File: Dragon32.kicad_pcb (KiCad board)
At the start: 2 copper layers, 253 x 169.1 mm, 142 parts, among them IC1 4164, IC15 MC6883, IC16 74LS244N, IC17 27C256, IC18 74LS08, IC19 MC6809E, IC2 4164, IC20 MC14529B, IC24 74LS244N, IC25 LM393P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

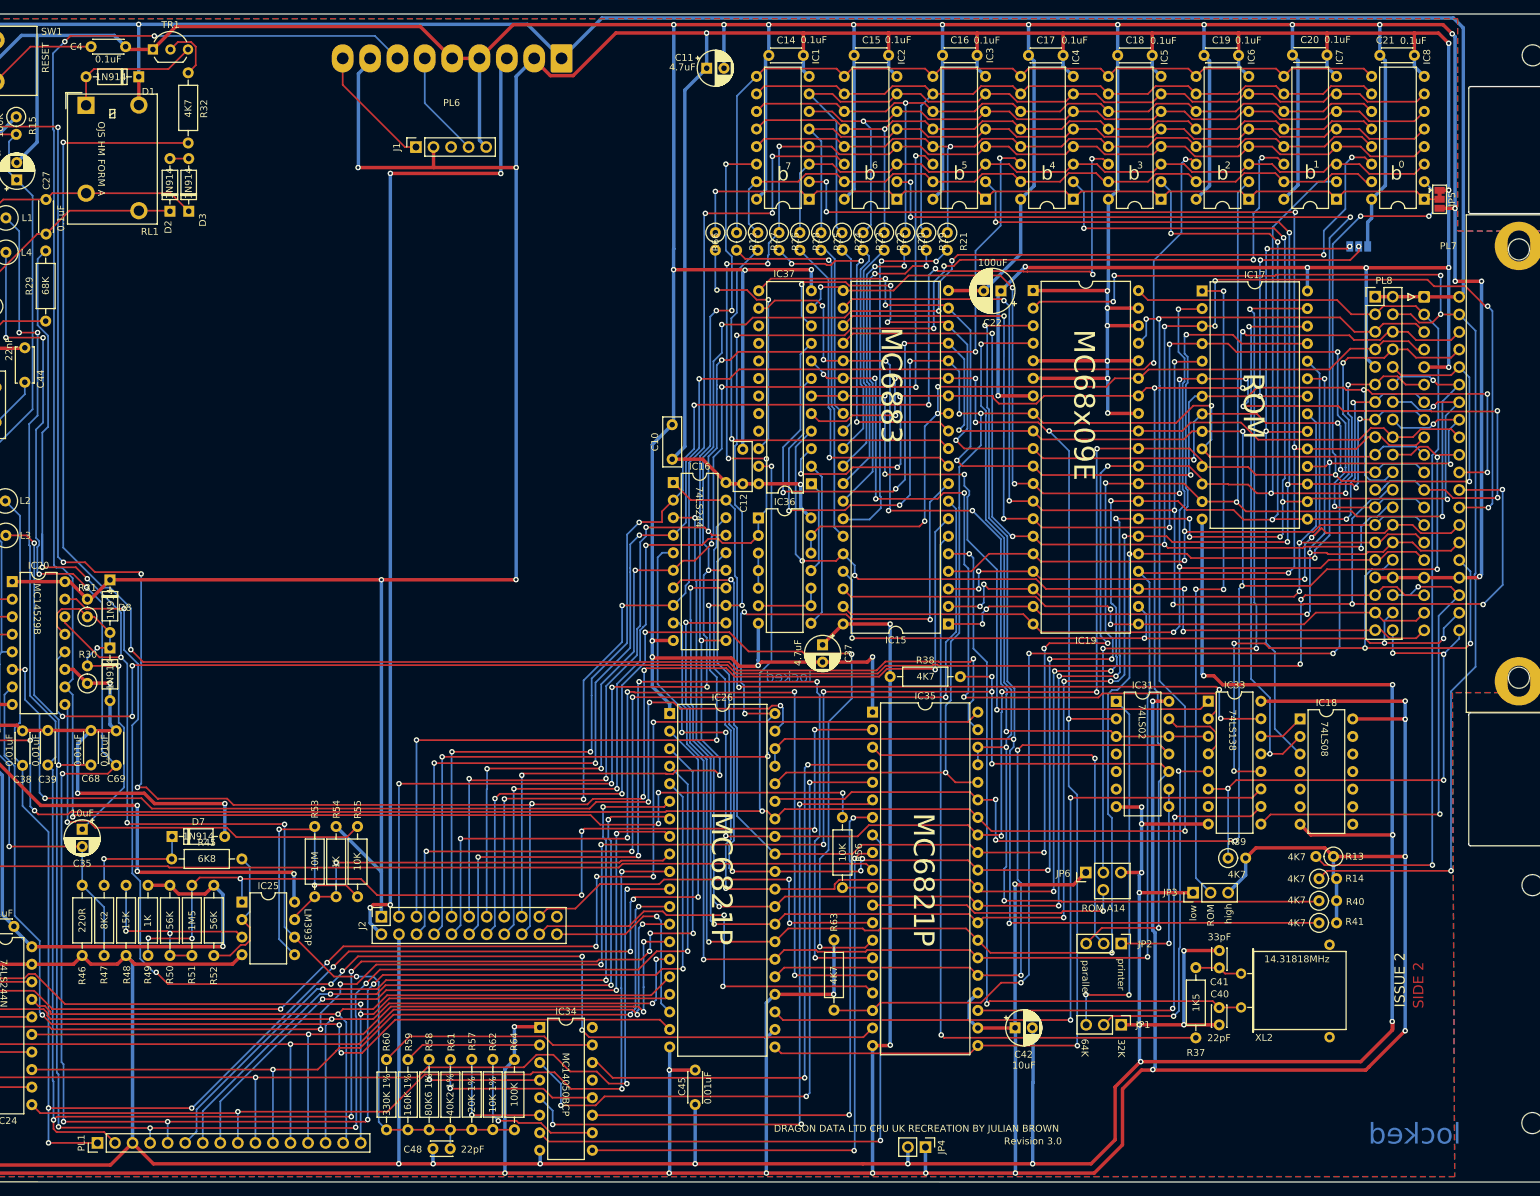
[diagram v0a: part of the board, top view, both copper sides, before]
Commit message: add control for pia 3
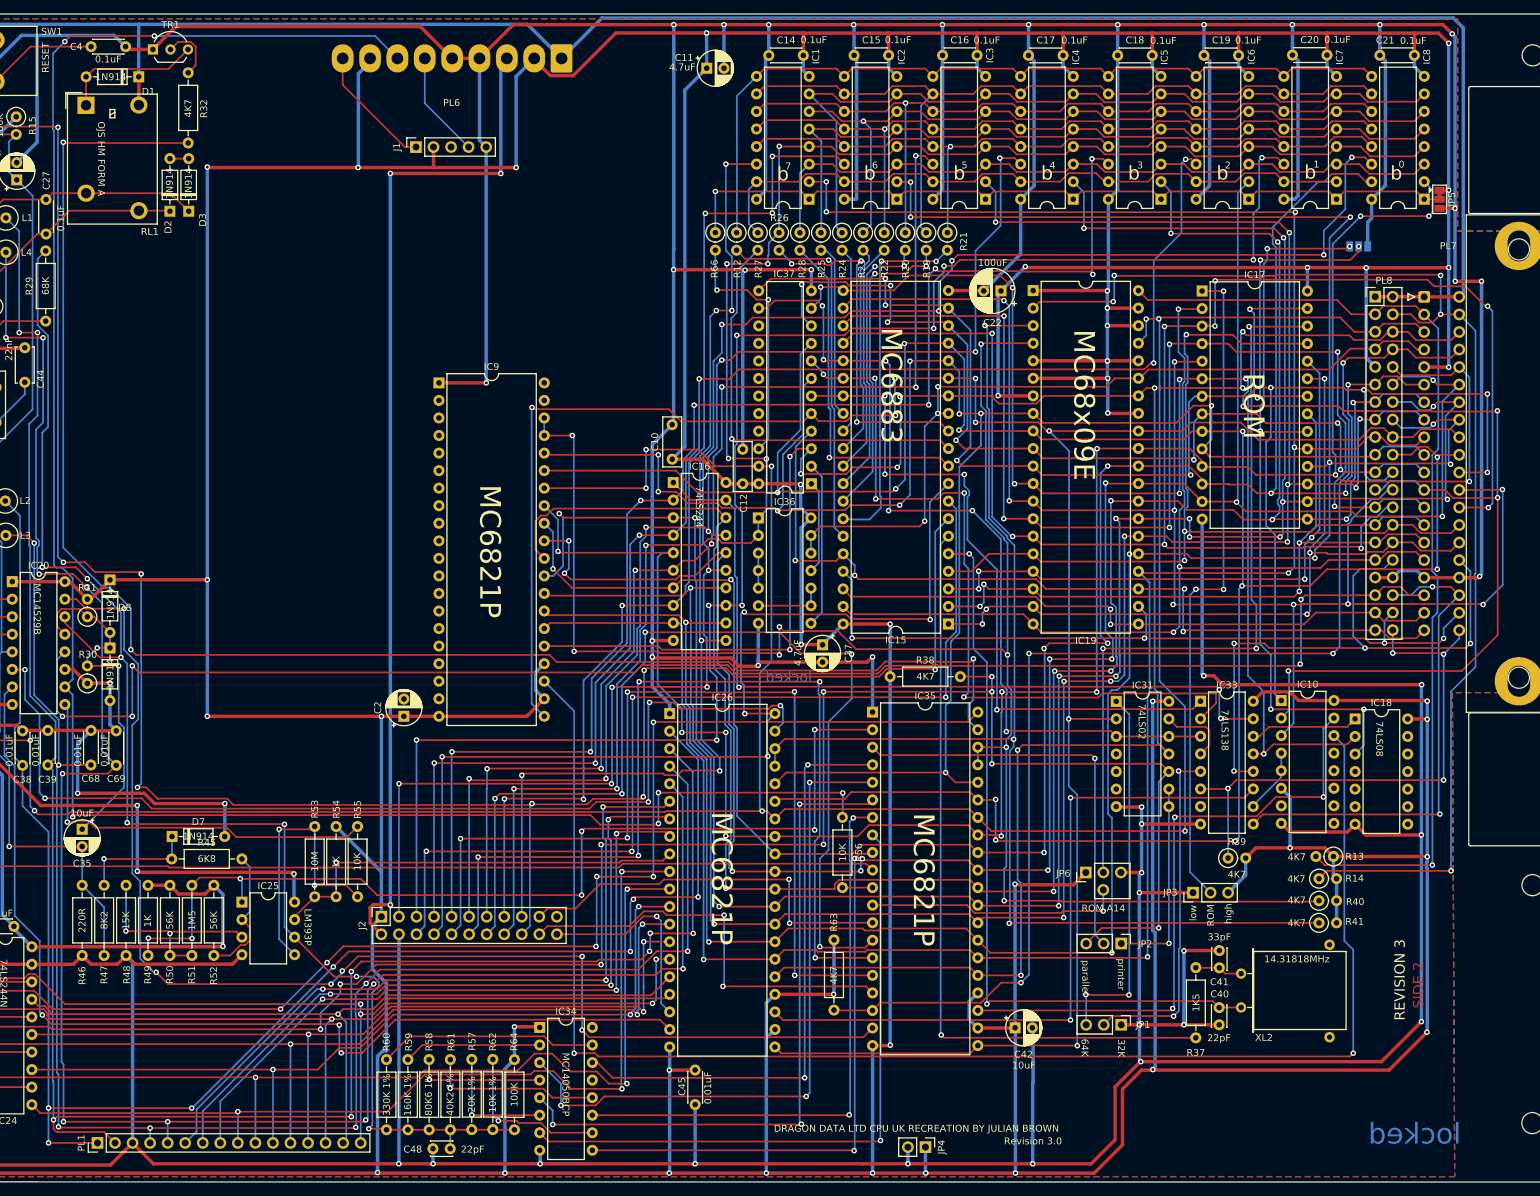
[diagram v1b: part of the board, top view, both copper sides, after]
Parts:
- added C2: 10uF, Capacitor_THT:CP_Radial_D5.0mm_P2.50mm, F.Cu at (158.0, 133.3)
- added IC10: 74LS138, Package_DIP:DIP-16_W7.62mm, F.Cu at (285.0, 131.1)
- added IC9: MC6821, Package_DIP:DIP-40_W15.24mm, F.Cu at (163.1, 85.1)
- moved IC18 7.96 mm to (295.7, 133.7)
- moved IC33 1.12 mm to (273.3, 131.2)
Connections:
- IC35 pad 23: P1 -> P1a
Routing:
- net P1b: track 0.00 -> 215.9 mm, vias 0 -> 2
- net +5V: track 1627.5 -> 1738.4 mm, vias 39 -> 44
- net ~{FIRQ}: track 142.8 -> 249.4 mm, vias 3 -> 8
- net P1a: track 0.00 -> 90.9 mm, vias 0 -> 3
- net R/~{W}: track 252.9 -> 340.1 mm, vias 7 -> 8
- net E: track 268.0 -> 335.3 mm, vias 8 -> 10
- net P1: track 69.2 -> 9.40 mm, vias 2 -> 0
- net A4: track 186.1 -> 245.7 mm, vias 9 -> 10
- net GND: track 1774.3 -> 1831.4 mm, vias 56 -> 57
- net A3: track 178.9 -> 225.4 mm, vias 7 -> 8
- net A0: track 235.7 -> 278.3 mm, vias 7 -> 9
- net ~{RES}: track 461.8 -> 499.4 mm, vias 8 -> 10
- net A1: track 313.6 -> 349.8 mm
- net D3: track 298.9 -> 334.1 mm
- net D2: track 290.3 -> 324.2 mm, vias 10 -> 12
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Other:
- board text added: "REVISION 3"
- board text removed: "ISSUE 2"

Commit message: add power pin to keyboard connection
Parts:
- PL1: value Conn_01x16_Male -> Conn_01x18_Pin; footprint Connector_PinHeader_2.54mm:PinHeader_1x16_P2.54mm_Vertical -> Connector_PinHeader_2.54mm:PinHeader_1x18_P2.54mm_Vertical
- moved PL1 5.08 mm to (108.6, 195.1)
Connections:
- PL1 pad 1: PA0 -> +5V
- PL1 pad 10: PB1 -> PA6
- PL1 pad 11: PB2 -> PB0
- PL1 pad 12: PB3 -> PB1
- PL1 pad 13: PB4 -> PB2
- PL1 pad 14: PB5 -> PB3
- PL1 pad 15: PB6 -> PB4
- PL1 pad 16: PB7 -> PB5
- PL1 pad 2: PA1 -> unconnected-(PL1-Pin_2-Pad2)
- PL1 pad 3: GND -> PA0
- PL1 pad 4: PA2 -> PA1
- PL1 pad 5: PA3 -> GND
- PL1 pad 6: PA4 -> PA2
- PL1 pad 7: PA5 -> PA3
- PL1 pad 8: PA6 -> PA4
- PL1 pad 9: PB0 -> PA5
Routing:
- net +5V: track 1738.4 -> 1742.8 mm, vias 44 -> 45
- net PA0: track 239.8 -> 242.5 mm
- net GND: track 1831.4 -> 1833.1 mm
- net DA0: track 139.5 -> 140.9 mm
- net AD1: track 148.3 -> 149.5 mm
- net ~{HALT}: track 142.7 -> 143.8 mm
- net GM2: track 136.3 -> 137.3 mm
- net GM1: track 135.2 -> 136.2 mm
- net DO0: track 248.2 -> 247.5 mm
- net A1: track 349.8 -> 349.1 mm
- net 6bit D/A: track 203.6 -> 203.1 mm

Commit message: complete tracing for fabrication
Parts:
- added J3: Conn_02x08_Odd_Even, Connector_PinSocket_2.54mm:PinSocket_2x08_P2.54mm_Vertical, F.Cu at (101.0, 125.1)
- moved IC9 27.6 mm to (135.5, 85.2)
- moved C2 26.7 mm to (131.3, 133.3), turned to -90 degrees
- moved D9 11.3 mm to (126.7, 123.4)
- moved D8 11.3 mm to (126.7, 113.6)
- moved C38 8.97 mm to (111.8, 135.3)
- moved C39 8.23 mm to (114.7, 135.3)
- moved R31 7.97 mm to (120.1, 118.9)
- moved C35 7.95 mm to (119.4, 149.9)
- moved R30 7.84 mm to (120.0, 128.6)
- moved IC20 7.53 mm to (108.8, 113.8)
- moved R42 5.72 mm to (96.0, 145.7)
- moved R43 5.72 mm to (92.8, 145.7)
- moved C1 5.16 mm to (84.4, 123.9)
- moved C30 5.16 mm to (84.4, 126.9)
- moved C31 5.16 mm to (84.4, 129.9)
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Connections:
- IC9 pad 10: unconnected-(IC9-PB0-Pad10) -> Alpha
- IC9 pad 11: unconnected-(IC9-PB1-Pad11) -> Inverse
- IC9 pad 12: unconnected-(IC9-PB2-Pad12) -> ~{SelInv}
- IC9 pad 13: unconnected-(IC9-PB3-Pad13) -> RClk
- IC9 pad 14: unconnected-(IC9-PB4-Pad14) -> RC
- IC9 pad 2: unconnected-(IC9-PA0-Pad2) -> DC0
- IC9 pad 3: unconnected-(IC9-PA1-Pad3) -> DC1
- IC9 pad 4: unconnected-(IC9-PA2-Pad4) -> DC2
- IC9 pad 5: unconnected-(IC9-PA3-Pad5) -> DC3
- IC9 pad 6: unconnected-(IC9-PA4-Pad6) -> DC4
- IC9 pad 7: unconnected-(IC9-PA5-Pad7) -> DC5
- IC9 pad 8: unconnected-(IC9-PA6-Pad8) -> DC6
- IC9 pad 9: unconnected-(IC9-PA7-Pad9) -> DC7
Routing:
- net DC7: track 0.00 -> 67.8 mm, vias 0 -> 1
- net GND: track 1833.1 -> 1766.5 mm, vias 57 -> 55
- net DC6: track 0.00 -> 65.9 mm, vias 0 -> 1
- net DC5: track 0.00 -> 65.2 mm, vias 0 -> 1
- net DC4: track 0.00 -> 64.1 mm, vias 0 -> 1
- net DC3: track 0.00 -> 62.9 mm, vias 0 -> 1
- net DC2: track 0.00 -> 62.2 mm, vias 0 -> 1
- net DC1: track 0.00 -> 59.8 mm, vias 0 -> 1
- net DC0: track 0.00 -> 59.1 mm, vias 0 -> 1
- net Alpha: track 0.00 -> 58.5 mm, vias 0 -> 1
- net Inverse: track 0.00 -> 57.9 mm, vias 0 -> 1
- net ~{SelInv}: track 0.00 -> 54.8 mm, vias 0 -> 1
- net RClk: track 0.00 -> 54.3 mm, vias 0 -> 1
- net RC: track 0.00 -> 51.7 mm, vias 0 -> 1
- net ~{RES}: track 499.4 -> 530.5 mm
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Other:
- board text added: "Alpha 1"
